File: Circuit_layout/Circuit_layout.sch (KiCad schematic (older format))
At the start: 27 parts, among them U15 TLP293, U17 MCP6004, U7 AT90CAN128-A, U9 TLP293, Y1 10MHz

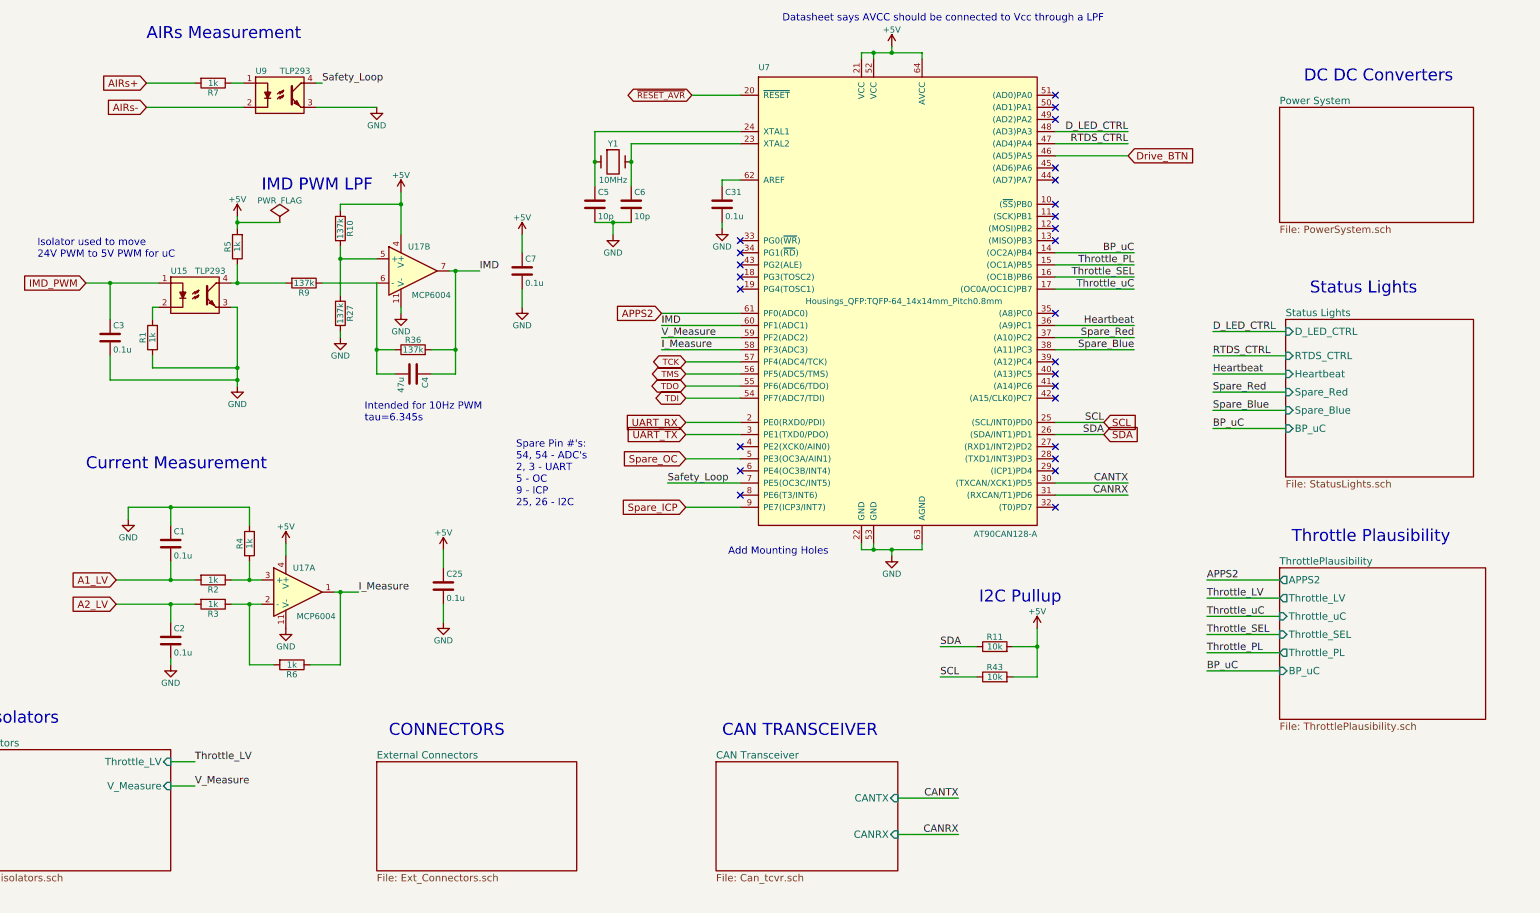
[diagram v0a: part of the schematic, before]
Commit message: added watchdog to schematic, added avr datasheet
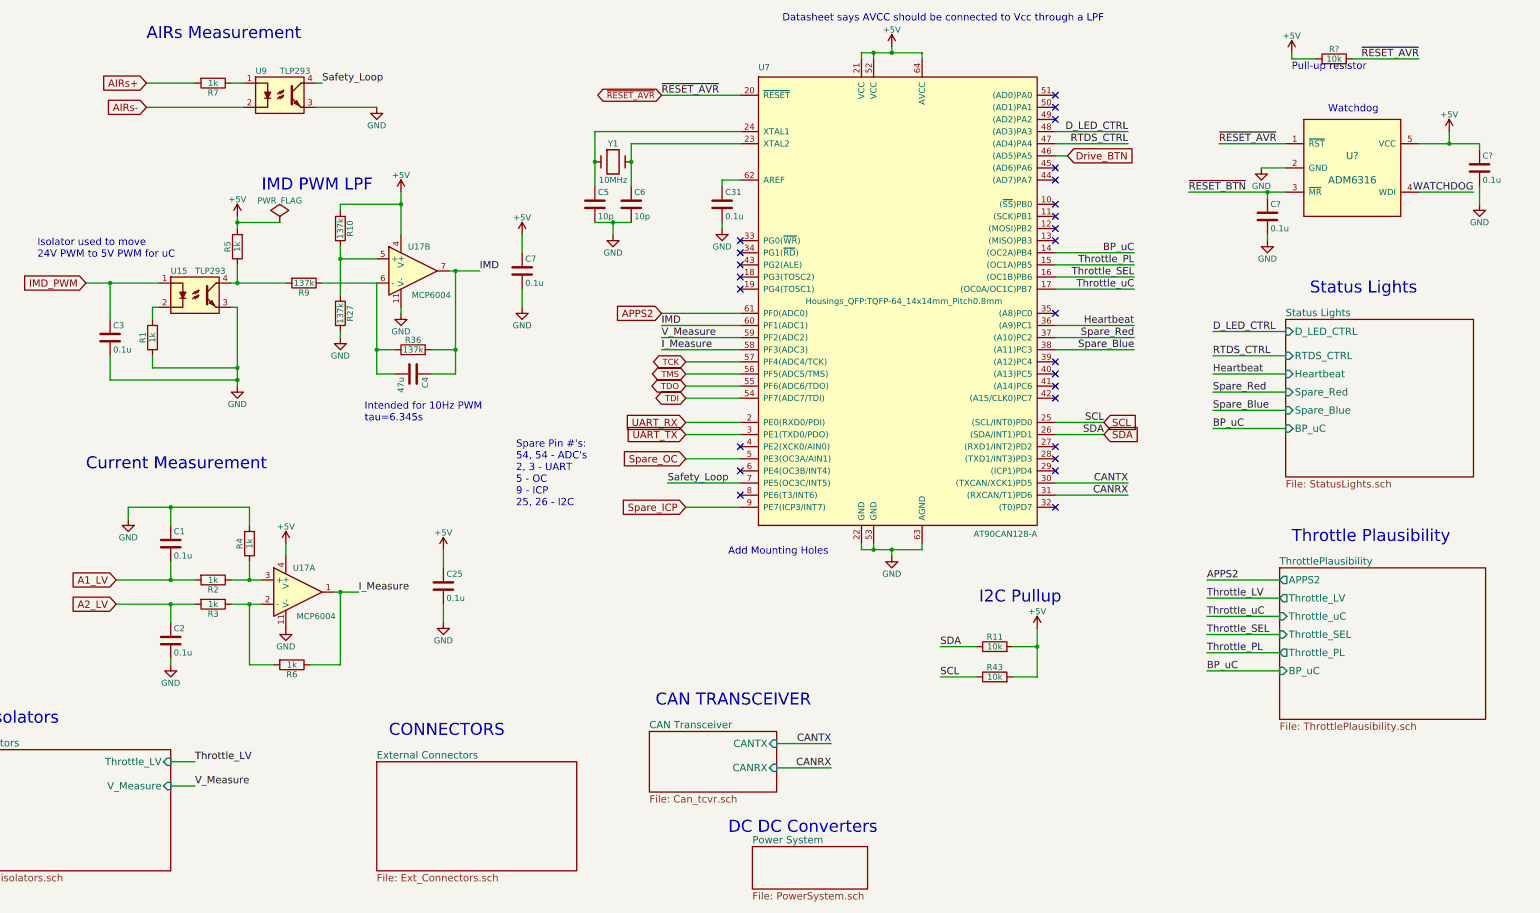
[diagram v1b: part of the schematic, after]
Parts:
- added C? (x2): 0.1u, Capacitors_SMD:C_0805_HandSoldering, symbol C
- added R?: 10k, Resistors_SMD:R_0805_HandSoldering, symbol R
- added U?: ADM6316, symbol ADM6316
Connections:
- net +5V: now also C?.1, R?.1, U?.5 (VCC)
- net GND: now also C?.2, C?.2, U?.2 (GND)
- net ~RESET_AVR: now also R?.2, U?.1 (~RST)
- new net WATCHDOG: U?.4 (WDI)
- new net ~RESET_BTN: C?.1, U?.3 (~MR)
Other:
- note added: "Pull-up resistor"
- note added: "Watchdog"

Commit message: added all info for LDO, except footprint. need to add step-down for brake overtravel
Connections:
- net BOT_uC: now reaches U7.35 ((A8)PC0)
- no-connect marks 26 -> 25
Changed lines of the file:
@@
 F6 "BP_uC" I L 11600 6000 60
 F7 "Throttle_PL" O L 11600 5850 60
+F8 "BOT_uC" I L 11600 6150 60
 $EndSheet
 Text Notes 1750 4350 0    99   ~ 0
@@
 NoConn ~ 9750 2350
 NoConn ~ 9750 2450
-NoConn ~ 9750 3050
 NoConn ~ 9750 3450
 NoConn ~ 9750 3550
@@
 Text Notes 12000 1400 0    60   ~ 0
 Watchdog
+Wire Wire Line
+	11000 6150 11600 6150
+Text Label 11000 6150 0    60   ~ 0
+BOT_uC
+Wire Wire Line
+	9750 3050 10400 3050
+Text Label 10400 3050 2    60   ~ 0
+BOT_uC
 $EndSCHEMATC

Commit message: need to make further changes after review w/ prof
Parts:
- removed C3: 0.1u, Capacitors_SMD:C_0805_HandSoldering, symbol C
- removed R1, R7: 1k, Resistors_SMD:R_0805_HandSoldering, symbol R
- added R? (x2): 10k, Resistors_SMD:R_0805_HandSoldering, symbol R
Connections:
- net AIRs+: now also R?.2
- net GND: now also R?.2
- net at U9.1: now also R?.1
- net at U15.2: now also R?.1
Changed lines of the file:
@@
 Text Label 3700 1150 0    60   ~ 0
 Safety_Loop
-$Comp
-L R R7
-U 1 1 58B4C950
-P 2800 1150
-F 0 "R7" V 2880 1150 50  0000 C CNN
-F 1 "1k" V 2800 1150 50  0000 C CNN
-F 2 "Resistors_SMD:R_0805_HandSoldering" V 2730 1150 50  0001 C CNN
-F 3 "" H 2800 1150 50  0000 C CNN
-F 4 "P1.00KCCT-ND" V 2800 1150 60  0001 C CNN "DigiKey P/N"
-F 5 "http://www.digikey.com/product-detail/en/panasonic-electronic-components/ERJ-6ENF1001V/P1.00KCCT-ND/118957" V 2800 1150 60  0001 C CNN "URL"
-F 6 "ERJ-6ENF1001V" V 2800 1150 60  0001 C CNN "Man P/N"
-	1    2800 1150
-	0    1    1    0
-$EndComp
 Text Label 6550 4450 0    60   ~ 0
 Safety_Loop
@@
 $EndComp
 $Comp
-L C C3
-U 1 1 58BC8705
-P 1950 3250
-F 0 "C3" H 1975 3350 50  0000 L CNN
-F 1 "0.1u" H 1975 3150 50  0000 L CNN
-F 2 "Capacitors_SMD:C_0805_HandSoldering" H 1988 3100 50  0001 C CNN
-F 3 "http://www.kemet.com/Lists/ProductCatalog/Attachments/53/KEM_C1002_X7R_SMD.pdf" H 1950 3250 50  0001 C CNN
-F 4 "399-1168-1-ND" H 1950 3250 60  0001 C CNN "Digikey P/N"
-F 5 "http://www.digikey.com/product-detail/en/kemet/C0805C104K3RACTU/399-1168-1-ND/411443" H 1950 3250 60  0001 C CNN "URL"
-F 6 "C0805C104K3RACTU" H 1950 3250 60  0001 C CNN "Man P/N"
-	1    1950 3250
-	1    0    0    -1
-$EndComp
-$Comp
 L C C7
 U 1 1 58BC98BF
@@
 	1    2650 2900
 	1    0    0    -1
-$EndComp
-$Comp
-L R R1
-U 1 1 58BB7DEE
-P 2300 3250
-F 0 "R1" V 2380 3250 50  0000 C CNN
-F 1 "1k" V 2300 3250 50  0000 C CNN
-F 2 "Resistors_SMD:R_0805_HandSoldering" V 2230 3250 50  0001 C CNN
-F 3 "" H 2300 3250 50  0000 C CNN
-F 4 "P1.00KCCT-ND" V 2300 3250 60  0001 C CNN "DigiKey P/N"
-F 5 "http://www.digikey.com/product-detail/en/panasonic-electronic-components/ERJ-6ENF1001V/P1.00KCCT-ND/118957" V 2300 3250 60  0001 C CNN "URL"
-F 6 "ERJ-6ENF1001V" V 2300 3250 60  0001 C CNN "Man P/N"
-	1    2300 3250
-	-1   0    0    1
 $EndComp
 $Comp
@@
 Connection ~ 3000 3500
 Wire Wire Line
-	1950 3400 1950 3600
-Wire Wire Line
-	1950 3600 3000 3600
-Connection ~ 3000 3600
-Wire Wire Line
-	1950 2800 1950 3100
-Connection ~ 1950 2800
-Wire Wire Line
 	3000 2300 3350 2300
 Connection ~ 3000 2300
@@
 Text Label 10400 3050 2    60   ~ 0
 BOT_uC
+$Comp
+L R R?
+U 1 1 58C138DA
+P 2300 3250
+F 0 "R?" V 2380 3250 50  0000 C CNN
+F 1 "10k" V 2300 3250 50  0000 C CNN
+F 2 "Resistors_SMD:R_0805_HandSoldering" V 2230 3250 50  0001 C CNN
+F 3 "" H 2300 3250 50  0000 C CNN
+F 4 "P10.0KCCT-ND" V 2300 3250 60  0001 C CNN "DigiKey P/N"
+F 5 "http://www.digikey.com/product-detail/en/panasonic-electronic-components/ERJ-6ENF1002V/P10.0KCCT-ND/119248" V 2300 3250 60  0001 C CNN "URL"
+F 6 "ERJ-6ENF1002V" V 2300 3250 60  0001 C CNN "Man P/N"
+	1    2300 3250
+	1    0    0    -1
+$EndComp
+$Comp
+L R R?
+U 1 1 58C14AF9
+P 2800 1150
+F 0 "R?" V 2880 1150 50  0000 C CNN
+F 1 "10k" V 2800 1150 50  0000 C CNN
+F 2 "Resistors_SMD:R_0805_HandSoldering" V 2730 1150 50  0001 C CNN
+F 3 "" H 2800 1150 50  0000 C CNN
+F 4 "P10.0KCCT-ND" V 2800 1150 60  0001 C CNN "DigiKey P/N"
+F 5 "http://www.digikey.com/product-detail/en/panasonic-electronic-components/ERJ-6ENF1002V/P10.0KCCT-ND/119248" V 2800 1150 60  0001 C CNN "URL"
+F 6 "ERJ-6ENF1002V" V 2800 1150 60  0001 C CNN "Man P/N"
+	1    2800 1150
+	0    1    1    0
+$EndComp
 $EndSCHEMATC

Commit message: modifiying hvpl
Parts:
- added SW?: SW_PUSH, symbol SW_PUSH
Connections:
- net GND: now also SW?.2
- net ~RESET_AVR: now also SW?.1
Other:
- note added: "Reset"
- moved on the sheet: C?, R11, R43, R?, U?

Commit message: changes before presentation
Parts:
- removed R2: 1k, Resistors_SMD:R_0805_HandSoldering, symbol R
- added R7: 10k, Resistors_SMD:R_0805_HandSoldering, symbol R
- R3, R4, R6: value 1k -> 10k; DigiKey P/N P1.00KCCT-ND -> P10.0KCCT-ND; Man P/N ERJ-6ENF1001V -> ERJ-6ENF1002V; URL http://www.digikey.com/product-detail/en/panasonic-electronic-components/ERJ-6ENF1001V/P1.00KCCT-ND/118957 -> http://www.digikey.com/product-detail/en/panasonic-electronic-components/ERJ-6ENF1002V/P10.0KCCT-ND/119248
- gave numbers to parts that had none: 7
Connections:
- net A1_LV: now also R3.2
- net A2_LV: now also R4.2; no longer R3.2
- net GND: now also R6.1; no longer R4.2
- net I_Measure: now also R7.1; no longer R6.1
- net at R3.1, R6.2: now also U17.3 (+); no longer U17.2 (-)
- net at R4.1: now also U17.2 (-), R7.2; no longer U17.3 (+)
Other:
- note removed: "Spare Pin #'s: \n54, 54 - ADC's\n2, 3 - UART\n5 - OC\n9 - ICP\n25, 26 - I2C\n"
- moved on the sheet: C1, C2, C25, U17A

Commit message: pics of schematic
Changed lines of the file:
@@
 LIBS:xilinx
 LIBS:Zilog
-LIBS:pacman-main-cache
 LIBS:bss84
 LIBS:+10v
@@
 	8150 4950 8150 5000
 Wire Wire Line
-	8150 5000 8250 5000
-Wire Wire Line
-	8250 5000 8400 5000
-Wire Wire Line
-	8400 5000 8650 5000
+	8150 5000 8650 5000
 Wire Wire Line
 	8250 5000 8250 4950
@@
 	8150 950  8150 900
 Wire Wire Line
-	8150 900  8250 900
-Wire Wire Line
-	8250 900  8400 900
-Wire Wire Line
-	8400 900  8650 900
+	8150 900  8650 900
 Wire Wire Line
 	8250 900  8250 950
@@
 Connection ~ 8400 900
 Wire Wire Line
-	6250 1650 6250 1800
-Wire Wire Line
-	6250 1800 6250 2000
+	6250 1650 6250 2000
 Wire Wire Line
 	6250 1650 7150 1650
@@
 	7150 1550 5950 1550
 Wire Wire Line
-	5950 1550 5950 1800
-Wire Wire Line
-	5950 1800 5950 2000
+	5950 1550 5950 2000
 Connection ~ 5950 1800
 Connection ~ 6250 1800
 Wire Wire Line
-	5950 2300 6100 2300
-Wire Wire Line
-	6100 2300 6250 2300
+	5950 2300 6250 2300
 Wire Wire Line
 	6100 2300 6100 2400
@@
 	9750 1750 9850 1750
 Wire Wire Line
-	3800 5250 3850 5250
-Wire Wire Line
-	3850 5250 4000 5250
-Wire Wire Line
-	2000 5150 2450 5150
-Wire Wire Line
-	2450 5150 2650 5150
-Wire Wire Line
-	2000 5350 2450 5350
-Wire Wire Line
-	2450 5350 2650 5350
+	3800 5250 4000 5250
+Wire Wire Line
+	2000 5150 2650 5150
+Wire Wire Line
+	2000 5350 2650 5350
 Wire Wire Line
 	3100 5350 3100 5850
 Wire Wire Line
-	2950 5350 3100 5350
-Wire Wire Line
-	3100 5350 3200 5350
+	2950 5350 3200 5350
 Wire Wire Line
 	3850 5250 3850 5850
@@
 Connection ~ 3100 5350
 Wire Wire Line
-	2950 5150 3100 5150
-Wire Wire Line
-	3100 5150 3200 5150
+	2950 5150 3200 5150
 Wire Wire Line
 	2450 5150 2450 5000
@@
 Connection ~ 2450 5350
 Wire Wire Line
-	2100 4550 2450 4550
-Wire Wire Line
-	2450 4550 3100 4550
+	2100 4550 3100 4550
 Wire Wire Line
 	2450 4550 2450 4700
@@
 	6500 3050 7150 3050
 Wire Wire Line
-	4350 2050 4350 2150
-Wire Wire Line
-	4350 2150 4350 2400
-Wire Wire Line
-	3850 2500 3850 2600
-Wire Wire Line
-	3850 2600 3850 2900
+	4350 2050 4350 2400
+Wire Wire Line
+	3850 2500 3850 2900
 Wire Wire Line
 	3850 2600 4150 2600
@@
 	4350 3000 4350 3050
 Wire Wire Line
-	4150 2800 4150 3350
-Wire Wire Line
-	4150 3350 4150 3550
+	4150 2800 4150 3550
 Wire Wire Line
 	4150 3350 4300 3350
@@
 	4600 3350 4800 3350
 Wire Wire Line
-	4800 2700 4800 3350
-Wire Wire Line
-	4800 3350 4800 3550
+	4800 2700 4800 3550
 Connection ~ 4800 2700
 Wire Wire Line
@@
 	3700 2800 4150 2800
 Wire Wire Line
-	4750 2700 4800 2700
-Wire Wire Line
-	4800 2700 5000 2700
+	4750 2700 5000 2700
 Wire Wire Line
 	5350 3000 5350 2850
@@
 	1750 2800 2350 2800
 Wire Wire Line
-	2950 2800 3000 2800
-Wire Wire Line
-	3000 2800 3400 2800
+	2950 2800 3400 2800
 Wire Wire Line
 	2350 3000 2300 3000
@@
 	2300 3000 2300 3100
 Wire Wire Line
-	3000 3000 3000 3500
-Wire Wire Line
-	3000 3500 3000 3650
+	3000 3000 3000 3650
 Wire Wire Line
 	3000 3000 2950 3000
@@
 	3000 2800 3000 2650
 Wire Wire Line
-	3000 2250 3000 2300
-Wire Wire Line
-	3000 2300 3000 2350
+	3000 2250 3000 2350
 Connection ~ 3000 2800
 Wire Wire Line
@@
 	12200 2500 12000 2500
 Wire Wire Line
-	12200 2100 12200 2250
-Wire Wire Line
-	12200 2250 12200 2500
+	12200 2100 12200 2500
 Wire Wire Line
 	12000 2250 12200 2250
@@
 	15950 2050 16150 2050
 Wire Wire Line
-	15350 2250 16000 2250
-Wire Wire Line
-	16000 2250 16150 2250
+	15350 2250 16150 2250
 Wire Wire Line
 	17250 2250 17700 2250
 Wire Wire Line
-	17250 1850 17500 1850
-Wire Wire Line
-	17500 1850 17750 1850
+	17250 1850 17750 1850
 Wire Wire Line
 	17750 1850 17750 1900
